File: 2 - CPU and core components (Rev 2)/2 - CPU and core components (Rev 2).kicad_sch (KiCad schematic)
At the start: 1 part

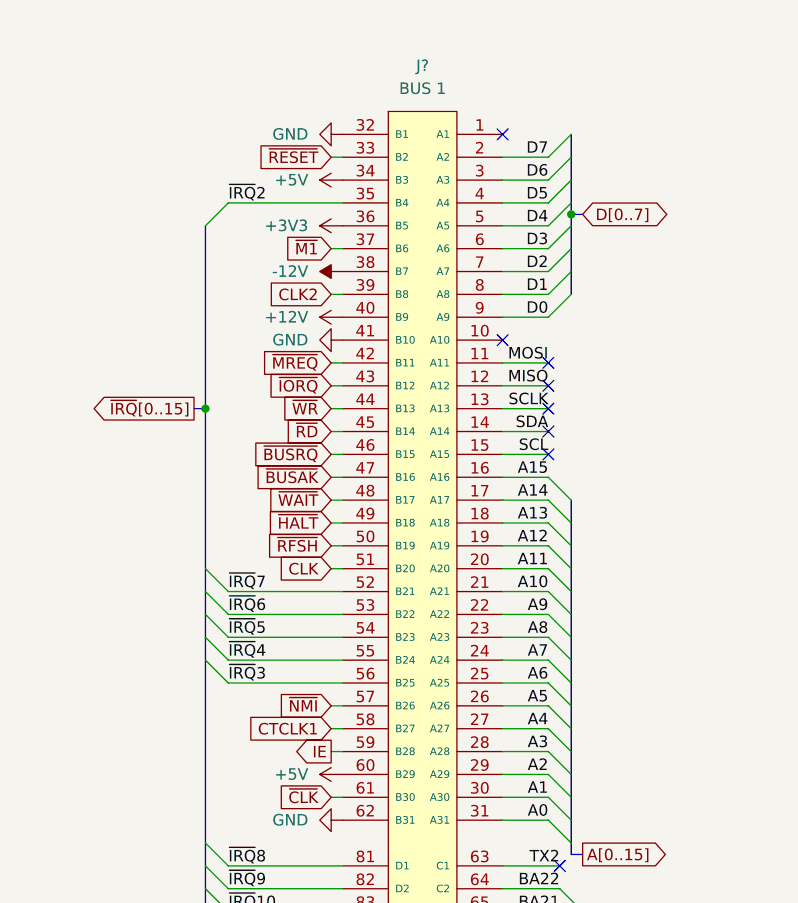
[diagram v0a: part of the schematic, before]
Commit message: Added Interrupt Enable daisy chain jumpers between the ISA slots
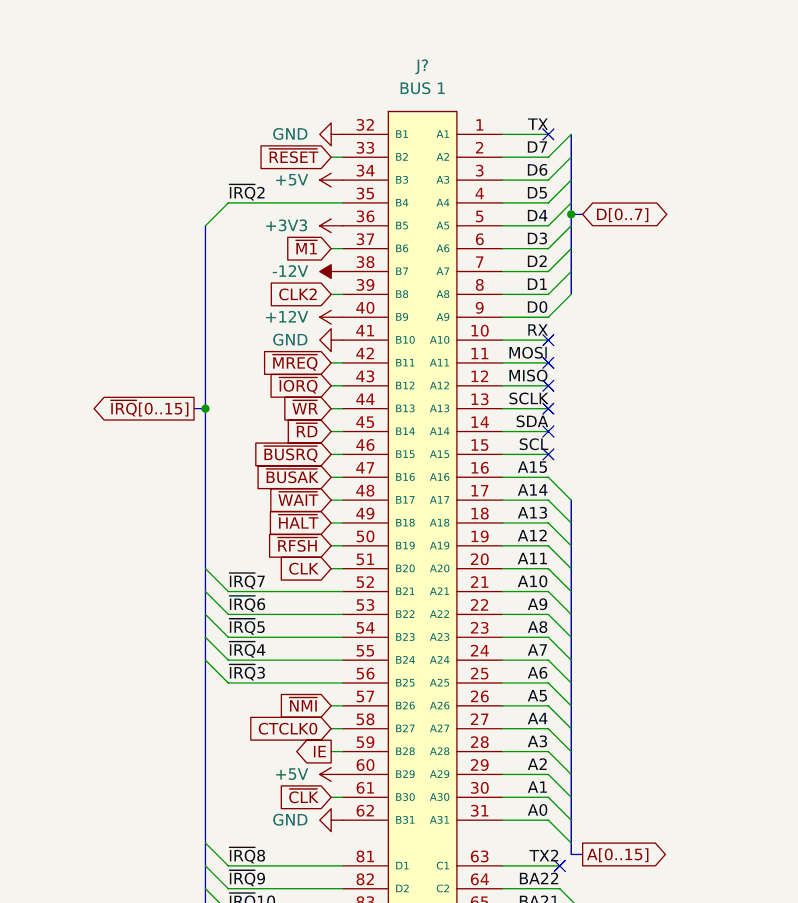
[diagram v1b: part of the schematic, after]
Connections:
- net TX: now reaches J?.1 (A1)
- net RX: now reaches J?.10 (A10)
- net CTCLK1 renamed CTCLK0
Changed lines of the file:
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@@
   (title_block
     (title "Core component card for ISA backplane")
-    (date "2023-08-27")
+    (date "2023-08-29")
     (rev "2")
     (company "Frédéric Segard")
@@
   (no_connect (at 71.12 78.74))
   (no_connect (at 72.39 154.94))
+  (no_connect (at 71.12 43.18))
   (no_connect (at 72.39 124.46))
   (no_connect (at 72.39 147.32))
@@
   (no_connect (at 72.39 162.56))
   (no_connect (at 72.39 167.64))
-  (no_connect (at 66.04 66.04))
   (no_connect (at 71.12 76.2))
   (no_connect (at 72.39 165.1))
-  (no_connect (at 66.04 43.18))
   (no_connect (at 40.64 154.94))
   (no_connect (at 40.64 149.86))
+  (no_connect (at 71.12 66.04))
   (no_connect (at 71.12 71.12))
   (no_connect (at 40.64 157.48))
@@
     (stroke (width 0) (type default))
   )
+  (wire (pts (xy 66.04 66.04) (xy 71.12 66.04))
+    (stroke (width 0) (type default))
+  )
   (bus (pts (xy 74.93 139.7) (xy 74.93 142.24))
     (stroke (width 0) (type default))
@@
     (stroke (width 0) (type default))
   )
+  (wire (pts (xy 66.04 43.18) (xy 71.12 43.18))
+    (stroke (width 0) (type default))
+  )
   (wire (pts (xy 66.04 55.88) (xy 71.12 55.88))
     (stroke (width 0) (type default))
@@
   (label "~{IRQ}14" (at 35.56 139.7 0) (fields_autoplaced)
     (effects (font (size 1.27 1.27)) (justify left bottom))
+  )
+  (label "RX" (at 71.12 66.04 180) (fields_autoplaced)
+    (effects (font (size 1.27 1.27)) (justify right bottom))
   )
   (label "A7" (at 71.12 101.6 180) (fields_autoplaced)
@@
   (label "~{IRQ}2" (at 35.56 50.8 0) (fields_autoplaced)
     (effects (font (size 1.27 1.27)) (justify left bottom))
+  )
+  (label "TX" (at 71.12 43.18 180) (fields_autoplaced)
+    (effects (font (size 1.27 1.27)) (justify right bottom))
   )
   (label "~{IRQ}6" (at 35.56 96.52 0) (fields_autoplaced)
@@
     )
   )
-  (global_label "CTCLK1" (shape input) (at 46.99 109.22 180) (fields_autoplaced)
+  (global_label "CTCLK0" (shape input) (at 46.99 109.22 180) (fields_autoplaced)
     (effects (font (size 1.27 1.27)) (justify right))
     (property "Intersheetrefs" "${INTERSHEET_REFS}" (at 36.9896 109.22 0)
